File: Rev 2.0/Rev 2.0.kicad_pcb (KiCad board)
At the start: 2 copper layers, 146.6 x 95 mm, 65 parts, among them J1 Conn_01x01_Pin, Q1 2n3904, Q2 IRF9540N, Q3 TIP31, Q6 2N3906, U4 TL494, U5 LM358, U6 TL431D

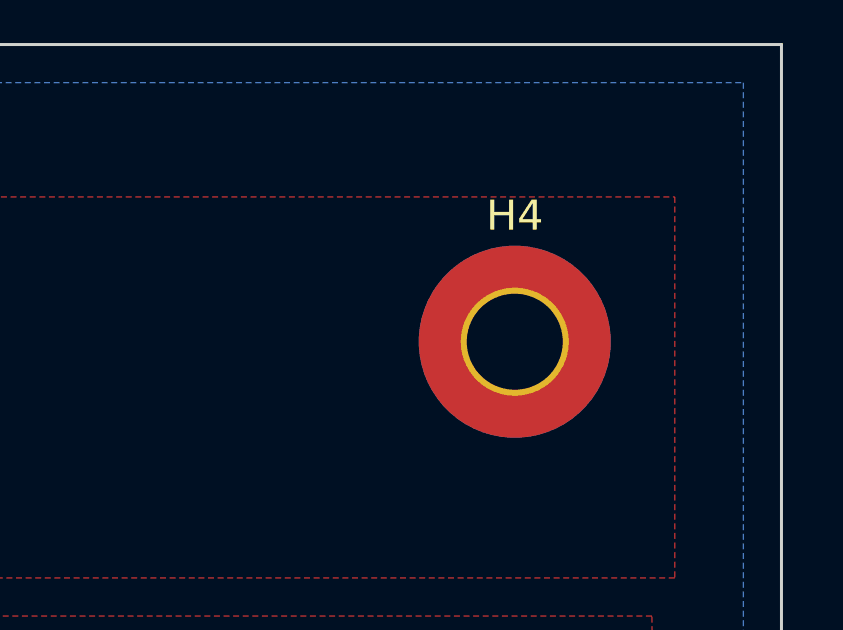
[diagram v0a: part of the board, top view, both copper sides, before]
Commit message: Reverted BAT- hole position
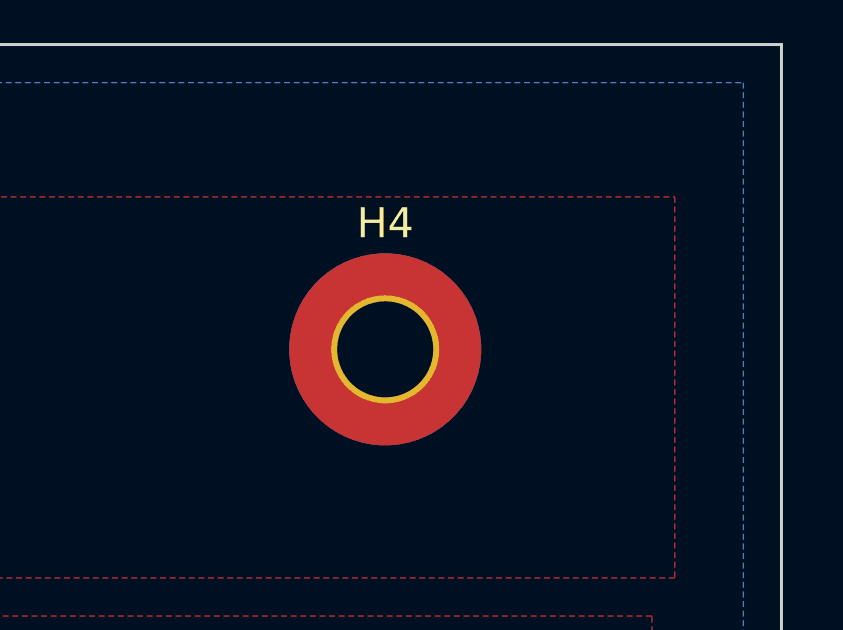
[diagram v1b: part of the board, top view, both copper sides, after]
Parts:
- moved H4 4.33 mm to (212.1, 55.9)
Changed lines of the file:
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@@
 		(tags "resistor handsolder")
 		(property "Reference" "R45"
-			(at -0.026 -1.65 360)
+			(at -0.026 -1.65 0)
 			(layer "F.SilkS")
 			(effects
@@
 		)
 		(property "Value" "2K"
-			(at 0 1.65 360)
+			(at 0 1.65 0)
 			(layer "F.Fab")
 			(effects
@@
 		)
 		(fp_text user "${REFERENCE}"
-			(at 0 0 360)
+			(at 0 0 0)
 			(layer "F.Fab")
 			(effects
@@
 		(tags "Through hole pin header THT 1x03 2.54mm single row")
 		(property "Reference" "RV2"
-			(at 0 -2.33 270)
+			(at 0 -2.33 -90)
 			(layer "F.SilkS")
 			(effects
@@
 		)
 		(property "Value" "20K"
-			(at 0 7.41 270)
+			(at 0 7.41 -90)
 			(layer "F.Fab")
 			(effects
@@
 		)
 		(fp_text user "${REFERENCE}"
-			(at 0 2.54 360)
+			(at 0 2.54 0)
 			(layer "F.Fab")
 			(effects
@@
 		(tags "resistor")
 		(property "Reference" "R4"
-			(at 0 -1.65 270)
+			(at 0 -1.65 -90)
 			(layer "F.SilkS")
 			(effects
@@
 		)
 		(property "Value" "220R"
-			(at 0 1.65 270)
+			(at 0 1.65 -90)
 			(layer "F.Fab")
 			(effects
@@
 		)
 		(fp_text user "${REFERENCE}"
-			(at 0 0 270)
+			(at 0 0 -90)
 			(layer "F.Fab")
 			(effects
@@
 	(footprint "MountingHole:MountingHole_3.2mm_M3_Pad_TopBottom"
 		(layer "F.Cu")
-		(at 216.408 55.626)
+		(at 212.09 55.88)
 		(descr "Mounting Hole 3.2mm, M3")
 		(tags "mounting hole 3.2mm m3")
@@
 		(tags "resistor")
 		(property "Reference" "R1"
-			(at 0 -1.65 270)
+			(at 0 -1.65 -90)
 			(layer "F.SilkS")
 			(effects
@@
 		)
 		(property "Value" "2k2"
-			(at 0 1.65 270)
+			(at 0 1.65 -90)
 			(layer "F.Fab")
 			(effects
@@
 		)
 		(fp_text user "${REFERENCE}"
-			(at 0 0 270)
+			(at 0 0 -90)
 			(layer "F.Fab")
 			(effects
@@
 		)
 		(fp_text user "${REFERENCE}"
-			(at 0 1.27 270)
+			(at 0 1.27 -90)
 			(layer "F.Fab")
 			(effects
@@
 		(tags "resistor handsolder")
 		(property "Reference" "R44"
-			(at 0.27 -1.65 360)
+			(at 0.27 -1.65 0)
 			(layer "F.SilkS")
 			(effects
@@
 		)
 		(property "Value" "10K"
-			(at 0 1.65 360)
+			(at 0 1.65 0)
 			(layer "F.Fab")
 			(effects
@@
 		)
 		(fp_text user "${REFERENCE}"
-			(at 0 0 360)
+			(at 0 0 0)
 			(layer "F.Fab")
 			(effects
@@
 		(tags "TO-220-3 Vertical RM 2.54mm")
 		(property "Reference" "Q2"
-			(at 2.54 -4.27 270)
+			(at 2.54 -4.27 -90)
 			(layer "F.SilkS")
 			(effects
@@
 		)
 		(property "Value" "IRF9540N"
-			(at 2.54 2.5 270)
+			(at 2.54 2.5 -90)
 			(layer "F.Fab")
 			(effects
@@
 		)
 		(fp_text user "${REFERENCE}"
-			(at 2.54 -4.27 270)
+			(at 2.54 -4.27 -90)
 			(layer "F.Fab")
 			(effects
@@
 		(tags "D_SOD-123F")
 		(property "Reference" "D11"
-			(at -0.127 -1.905 360)
+			(at -0.127 -1.905 0)
 			(layer "F.SilkS")
 			(effects
@@
 		)
 		(property "Value" "SZSMF4L15CAT3G"
-			(at 0 2.1 360)
+			(at 0 2.1 0)
 			(layer "F.Fab")
 			(effects
@@
 		)
 		(fp_text user "${REFERENCE}"
-			(at -0.127 -1.905 360)
+			(at -0.127 -1.905 0)
 			(layer "F.Fab")
 			(effects
@@
 		(tags "Diode DO-35_SOD27 series Axial Horizontal pin pitch 7.62mm  length 4mm diameter 2mm")
 		(property "Reference" "D4"
-			(at 3.81 -2.12 360)
+			(at 3.81 -2.12 0)
 			(layer "F.SilkS")
 			(effects
@@
 		)
 		(property "Value" "1N4148"
-			(at 3.81 2.12 360)
+			(at 3.81 2.12 0)
 			(layer "F.Fab")
 			(effects
@@
 		)
 		(fp_text user "K"
-			(at 0 -1.8 360)
+			(at 0 -1.8 0)
 			(layer "F.SilkS")
 			(effects
@@
 		)
 		(fp_text user "${REFERENCE}"
-			(at 4.11 0 360)
+			(at 4.11 0 0)
 			(layer "F.Fab")
 			(effects
@@
 		)
 		(fp_text user "K"
-			(at 0 -1.8 360)
+			(at 0 -1.8 0)
 			(layer "F.Fab")
 			(effects
@@
 		(tags "resistor handsolder")
 		(property "Reference" "R43"
-			(at 0 -1.65 360)
+			(at 0 -1.65 0)
 			(layer "F.SilkS")
 			(effects
@@
 		)
 		(property "Value" "2K2"
-			(at 0 1.65 360)
+			(at 0 1.65 0)
 			(layer "F.Fab")
 			(effects
@@
 		)
 		(fp_text user "${REFERENCE}"
-			(at 0 0 360)
+			(at 0 0 0)
 			(layer "F.Fab")
 			(effects
@@
 			(pts
 				(xy 177.546 82.296) (xy 177.546 78.994) (xy 207.518 78.994) (xy 207.518 86.106) (xy 172.212 86.106)
-				(xy 172.212 85.852) (xy 154.94 85.852) (xy 154.94 85.852) (xy 154.178 85.852) (xy 154.178 94.234)
-				(xy 152.4 94.234) (xy 152.4 94.996) (xy 147.574 94.996) (xy 147.574 97.028) (xy 143.51 97.028) (xy 143.51 97.028)
-				(xy 139.954 97.028) (xy 139.954 91.694) (xy 146.304 91.694) (xy 146.304 82.296)
+				(xy 172.212 85.852) (xy 154.94 85.852) (xy 154.178 85.852) (xy 154.178 94.234) (xy 152.4 94.234)
+				(xy 152.4 94.996) (xy 147.574 94.996) (xy 147.574 97.028) (xy 143.51 97.028) (xy 139.954 97.028)
+				(xy 139.954 91.694) (xy 146.304 91.694) (xy 146.304 82.296)
 			)
 		)
